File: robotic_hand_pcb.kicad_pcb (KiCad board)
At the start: 4 copper layers, 55 x 72.5 mm, 115 parts, among them J1 2171750001, J10 A6, J11 A7, J12 JST 1x5 Male, J13 JST 1x5 Male, J14 JST 1x5 Male, J15 JST 1x5 Male, J16 JST 1x5 Male, J2 TC2050-IDC, J4 UART, J5 A1, J6 A2, J7 A3, J8 A4, J9 A5, SW1 SPST, U1 LMR51430, U10 ACS712xLCTR-05B, U11 ACS712xLCTR-05B, U12 ACS712xLCTR-05B, U13 ACS712xLCTR-05B, U14 ULN2003ADR, U15 ULN2003ADR, U16 ULN2003ADR, U17 ULN2003ADR, U18 ULN2003ADR, U2 ld39150dt33-r, U3 TXB0104QPWRQ1, U4 STM32F446RET, U5 VL53L4CD, U7 BNO085, U8 ADS114S08, U9 ACS712xLCTR-05B, Y1 8M, Y2 32k768

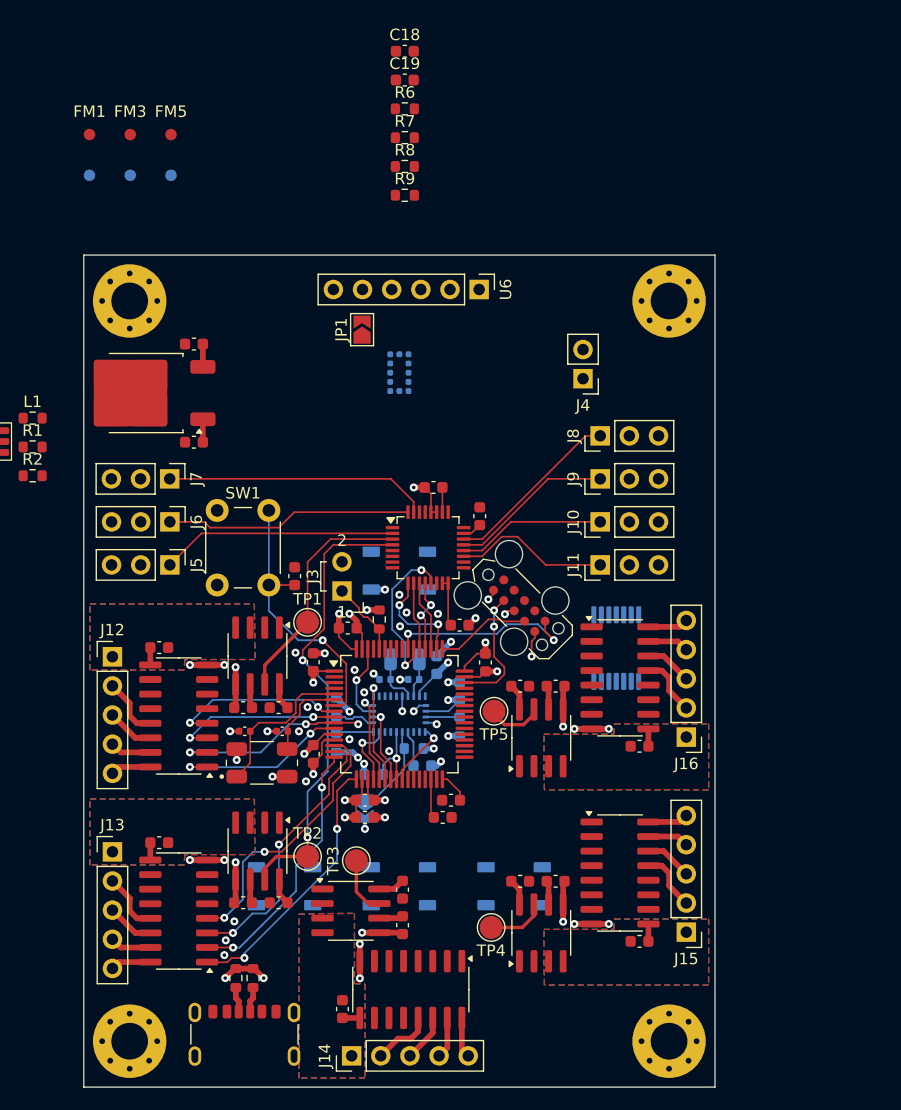
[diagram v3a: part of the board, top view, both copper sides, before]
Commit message: Update WIP, clean up stepper drivers
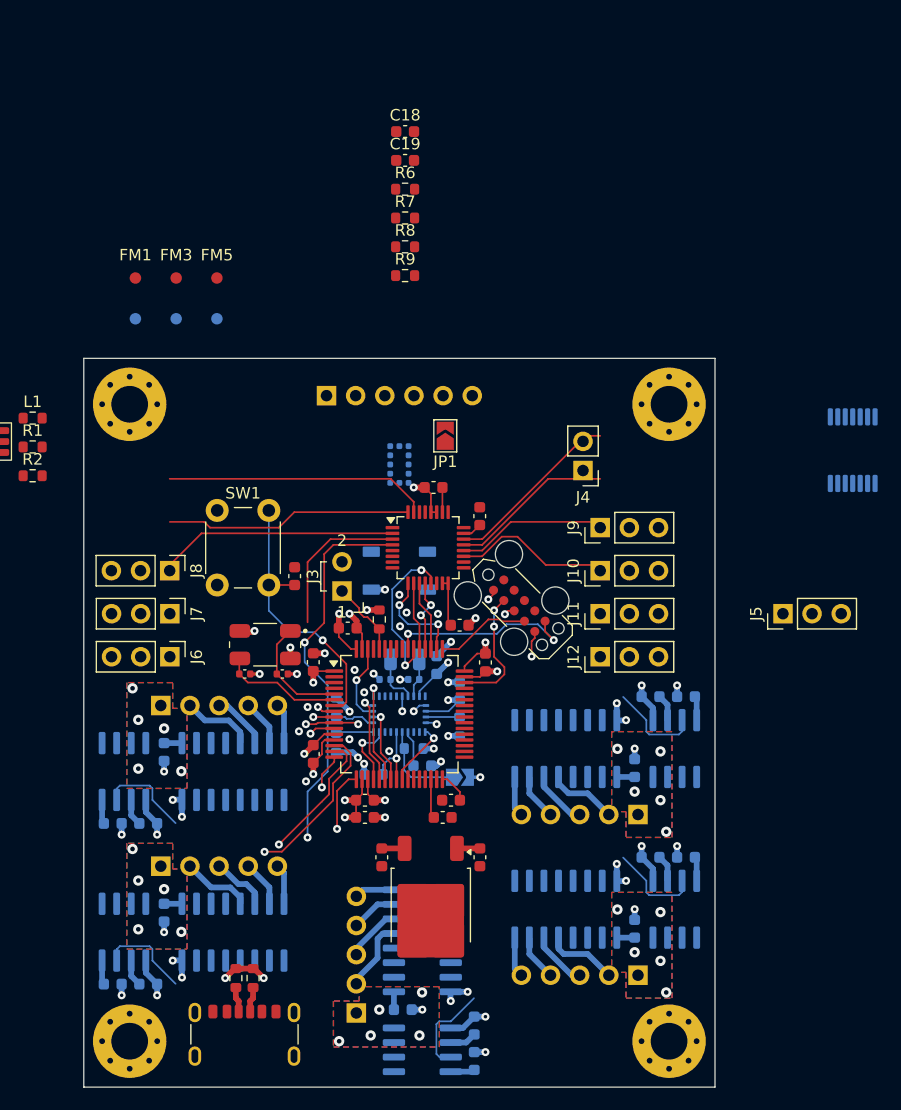
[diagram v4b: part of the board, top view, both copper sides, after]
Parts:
- removed D2, D3, D4: WS2812B, LED_SMD:LED_WS2812B_PLCC4_5.0x5.0mm_P3.2mm
- removed the J12 at (123.5, 100.0)
- removed the J16 at (173.5, 107.0)
- removed TP1, TP2, TP3, TP4, TP5: TestPoint, TestPoint:TestPoint_Pad_D2.0mm
- added J15: JST 1x5 Male, Connector_PinHeader_2.54mm:PinHeader_1x05_P2.54mm_Vertical, B.Cu at (144.8, 131.0)
- added J17: JST 1x5 Male, Connector_PinHeader_2.54mm:PinHeader_1x05_P2.54mm_Vertical, B.Cu at (169.3, 113.8)
- added J5: WS2812B, Connector_PinHeader_2.54mm:PinHeader_1x03_P2.54mm_Vertical, F.Cu at (181.9, 96.2)
- C28, C29, C30, C31, C32, C33, C34, C35, C36, C37, C38, C39, C40, C41, C42, J13, J14, U10, U11, U12, U13, U14, U15, U16, U17, U18, U6, U9: moved to B.Cu
- J16: renamed from J15; moved to B.Cu
- moved U2 51.2 mm to (151.2, 121.7), turned to -90 degrees
- moved C6 47.6 mm to (147.0, 117.5), turned to -90 degrees
- moved C5 43.9 mm to (155.5, 117.5), turned to -90 degrees
- moved U3 26.9 mm to (188.0, 82.0)
- moved J14 23.4 mm to (127.7, 118.2), turned to -90 degrees
- moved C28 17.6 mm to (123.5, 114.5), turned to 180 degrees
- moved U6 16.2 mm to (142.2, 77.2)
- moved C30 16.2 mm to (155.0, 135.2), turned to -90 degrees
- moved C29 16.1 mm to (123.5, 128.5), turned to 180 degrees
- moved U9 15.4 mm to (124.5, 110.0)
- moved C31 14.6 mm to (173.5, 117.5), turned to 0 degrees
- moved C32 14.5 mm to (173.5, 103.5), turned to 0 degrees
- moved U11 13.6 mm to (150.5, 134.2)
- moved U10 13.6 mm to (124.5, 124.0)
- moved J13 13.4 mm to (127.7, 104.2), turned to -90 degrees
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- renumbered J9 to J10, J10 to J11, J11 to J12, J5 to J6, J6 to J7, J7 to J8, J8 to J9
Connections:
- U14 pad 13: Net-(J12-Pin_2) -> Net-(J13-Pin_2)
- U14 pad 14: Net-(J12-Pin_3) -> Net-(J13-Pin_3)
- U14 pad 15: Net-(J12-Pin_4) -> Net-(J13-Pin_4)
- U14 pad 16: Net-(J12-Pin_5) -> Net-(J13-Pin_5)
- U15 pad 13: Net-(J13-Pin_2) -> Net-(J14-Pin_2)
- U15 pad 14: Net-(J13-Pin_3) -> Net-(J14-Pin_3)
- U15 pad 15: Net-(J13-Pin_4) -> Net-(J14-Pin_4)
- U15 pad 16: Net-(J13-Pin_5) -> Net-(J14-Pin_5)
- U16 pad 13: Net-(J14-Pin_2) -> Net-(J15-Pin_2)
- U16 pad 14: Net-(J14-Pin_3) -> Net-(J15-Pin_3)
- U16 pad 15: Net-(J14-Pin_4) -> Net-(J15-Pin_4)
- U16 pad 16: Net-(J14-Pin_5) -> Net-(J15-Pin_5)
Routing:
- net /M3_2: track 22.8 -> 3.09 mm, vias 2 -> 1
- net /M3_1: track 23.4 -> 5.42 mm, vias 2 -> 1
- net /M1_4: track 15.3 -> 1.58 mm, vias 2 -> 1
- net /M1_1: track 15.5 -> 2.26 mm, vias 2 -> 1
- net /M1_3: track 14.8 -> 1.82 mm, vias 2 -> 1
- net /M1_2: track 17.4 -> 4.83 mm, vias 3 -> 2
- net /M3_3: track 23.8 -> 11.5 mm, vias 2 -> 1
- net /M3_4: track 23.6 -> 14.3 mm, vias 2 -> 1
- net Net-(J15-Pin_2): track 0.00 -> 6.31 mm
- net GND: track 76.1 -> 81.4 mm, vias 55 -> 61
- net Net-(J12-Pin_2): track 5.30 -> 0.00 mm
- net Net-(J15-Pin_3): track 0.00 -> 4.88 mm
- net Net-(J12-Pin_3): track 4.12 -> 0.00 mm
- net Net-(J15-Pin_4): track 0.00 -> 4.04 mm
- net /HSE_IN: track 13.8 -> 9.98 mm
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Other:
- board size 55 x 72.5 mm -> 55 x 63.5 mm

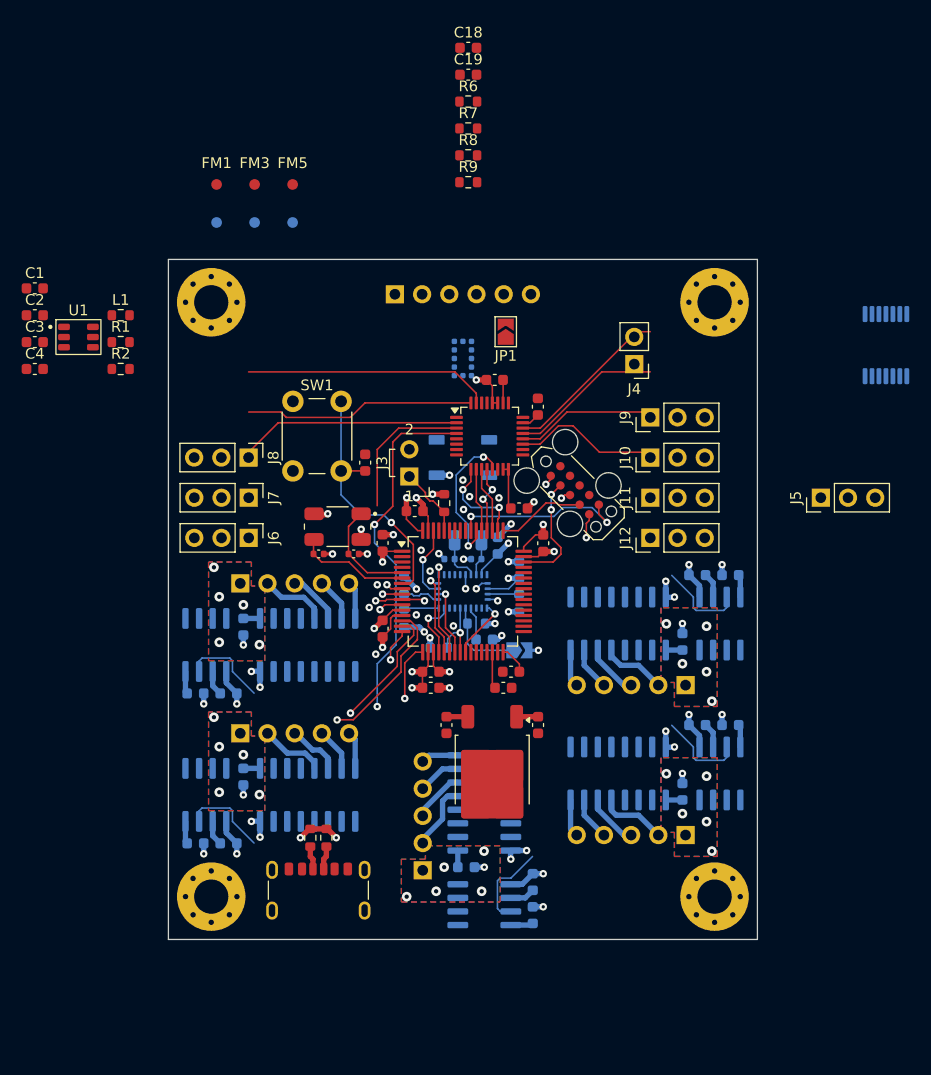
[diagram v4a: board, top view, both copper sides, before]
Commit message: Cleanup layout, add WIP routing
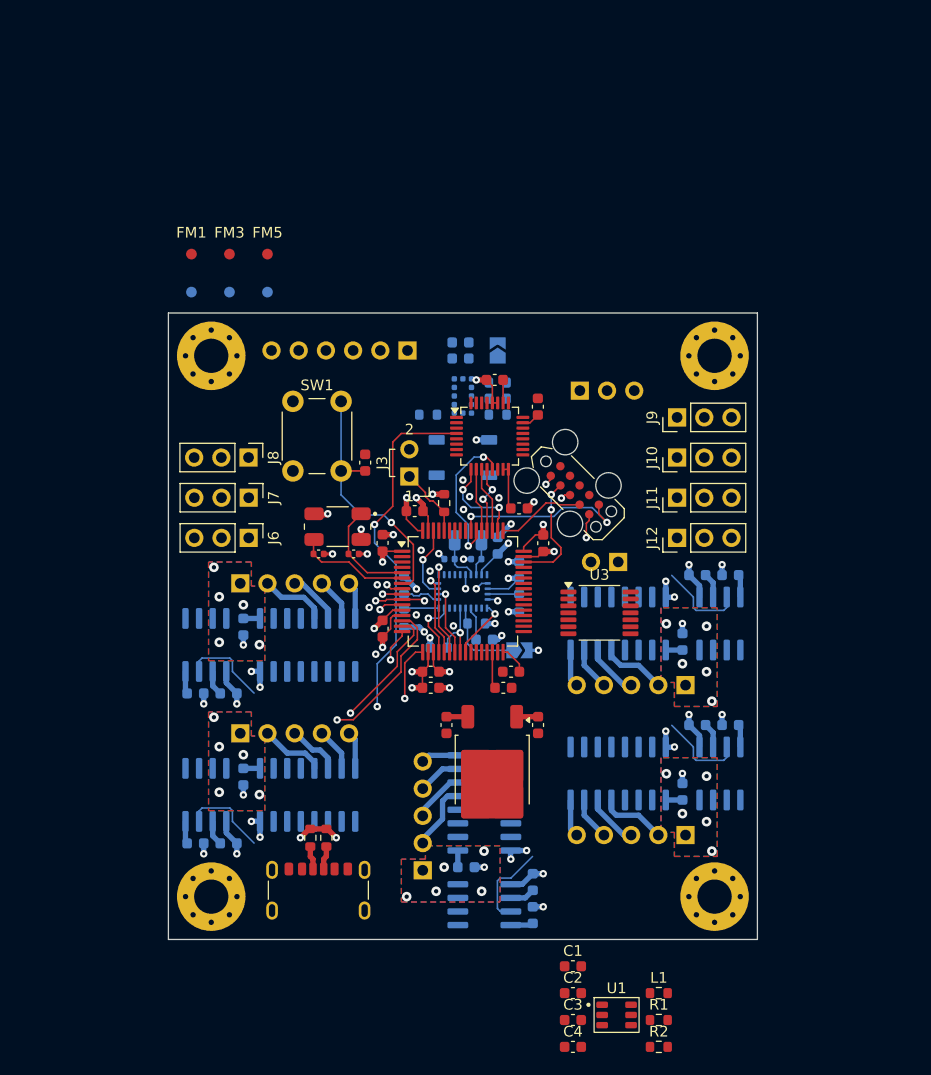
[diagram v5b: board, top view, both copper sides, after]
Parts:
- C18, C19, J4, J5, JP1, R6, R7, R8, R9: moved to B.Cu
- U3: moved to F.Cu
- moved C1 80.8 mm to (158.8, 140.0)
- moved C2 80.8 mm to (158.8, 142.5)
- moved C3 80.8 mm to (158.8, 145.0)
- moved C4 80.8 mm to (158.8, 147.5)
- moved R1 80.8 mm to (166.8, 145.0)
- moved U1 80.8 mm to (162.8, 144.6)
- moved L1 80.8 mm to (166.8, 142.5)
- moved R2 80.8 mm to (166.8, 147.5)
- moved U3 36.6 mm to (161.2, 107.0), turned to 0 degrees
- moved C18 29.0 mm to (148.3, 83.2)
- moved R6 27.9 mm to (151.8, 87.0), turned to 180 degrees
- moved C19 25.0 mm to (148.3, 81.8)
- moved J5 24.6 mm to (159.4, 86.2), turned to -90 degrees
- moved R8 24.5 mm to (145.2, 88.5)
- moved R7 23.9 mm to (151.8, 85.5)
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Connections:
- U3 pad 10: /TIM1_CH1_PWM_{5V} -> unconnected-(U3-B4-Pad10)
- U3 pad 13: unconnected-(U3-B1-Pad13) -> /TIM1_CH1_PWM_{5V}
- U3 pad 2: unconnected-(U3-A1-Pad2) -> /TIM1_CH1_PWM
- U3 pad 5: /TIM1_CH1_PWM -> unconnected-(U3-A4-Pad5)
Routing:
- net /robotic_hand_pcb_analog/ADC8: track 23.0 -> 0.00 mm
- net /robotic_hand_pcb_analog/ADC7: track 21.5 -> 0.00 mm
- net /robotic_hand_pcb_analog/ADC6: track 20.5 -> 0.00 mm
- net /robotic_hand_pcb_analog/ADC9: track 15.6 -> 0.00 mm
- net /robotic_hand_pcb_analog/ADC10: track 14.3 -> 0.00 mm
- net /robotic_hand_pcb_analog/ADC12: track 13.6 -> 0.00 mm
- net /robotic_hand_pcb_analog/ADC1: track 21.7 -> 8.17 mm
- net /robotic_hand_pcb_analog/ADC11: track 12.9 -> 0.00 mm
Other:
- board size 55 x 63.5 mm -> 55 x 58.5 mm

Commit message: Add minor layout improvements
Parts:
- J10, J11, J12, J6, J7, J8, J9: moved to B.Cu
- moved D1 18.9 mm to (164.5, 82.5)
- moved U3 17.6 mm to (163.5, 89.5), turned to 90 degrees
- moved C14 5.19 mm to (140.9, 88.0), turned to 90 degrees
- moved J5 4.81 mm to (159.0, 81.5), turned to 180 degrees
- moved J6 3.75 mm to (128.5, 96.2), turned to 90 degrees
- moved J7 3.75 mm to (128.5, 92.5), turned to 90 degrees
- moved J8 3.75 mm to (128.5, 88.8), turned to 90 degrees
- moved SW1 1.44 mm to (134.1, 93.8)
- turned J10 to -90 degrees
- turned J11 to -90 degrees
- turned J12 to -90 degrees
- turned J9 to -90 degrees
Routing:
- net /USART1_TX: track 0.00 -> 9.65 mm
- net /USART1_RX: track 0.00 -> 6.91 mm
- net /NRST: track 24.2 -> 22.5 mm

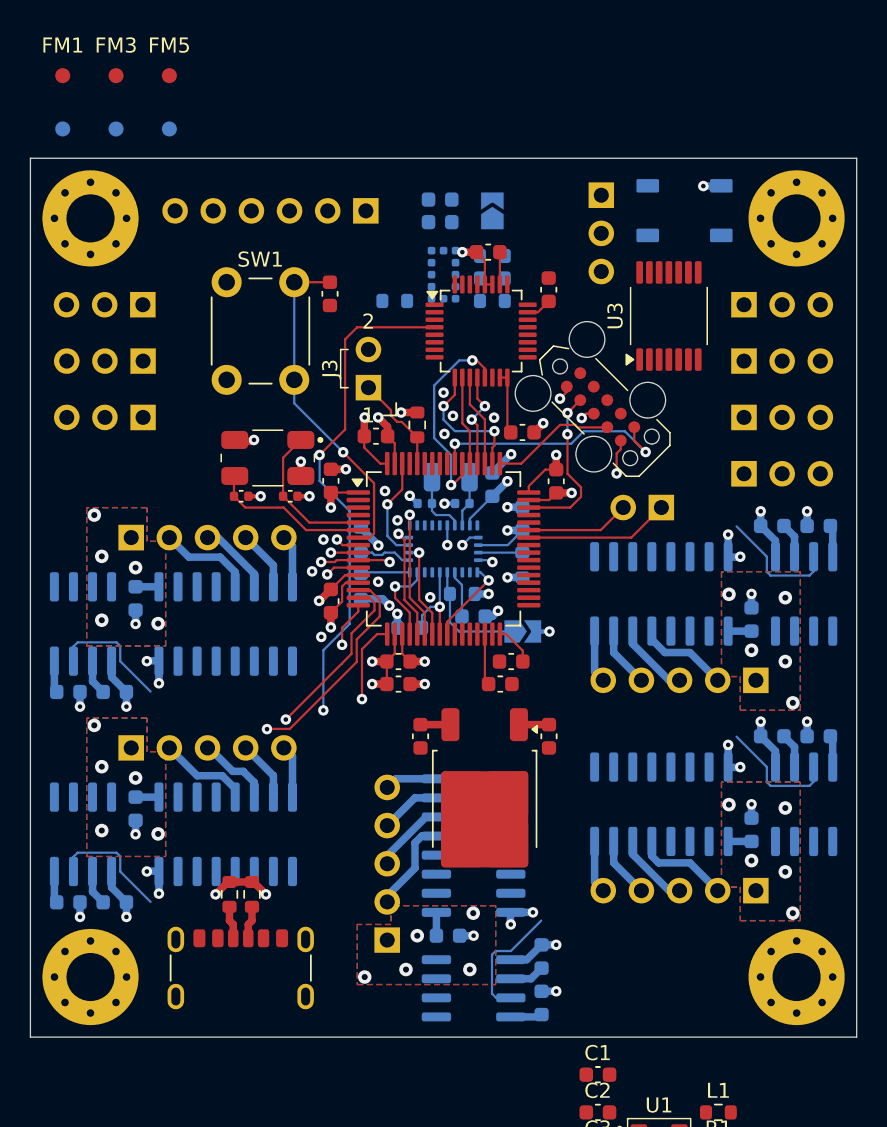
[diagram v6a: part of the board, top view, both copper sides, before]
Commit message: Route power, add major cleanup
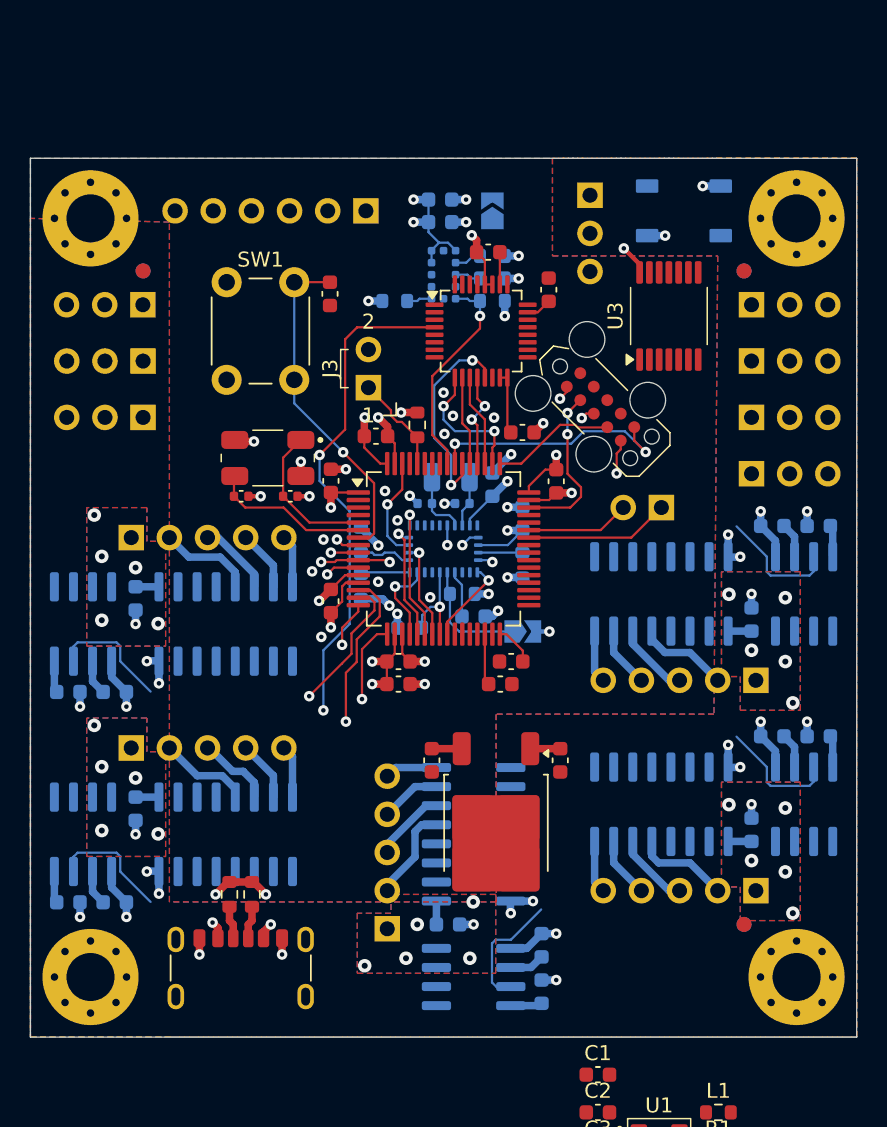
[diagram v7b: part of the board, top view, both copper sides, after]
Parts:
- FM2: moved to F.Cu
- FM5: moved to B.Cu
- moved FM3 70.3 mm to (168.5, 130.0)
- moved FM6 69.7 mm to (168.5, 130.0)
- moved FM4 42.9 mm to (168.5, 86.5)
- moved FM2 39.4 mm to (168.5, 86.5), turned to 0 degrees
- moved FM1 14.1 mm to (128.5, 86.5)
- moved FM5 13.1 mm to (128.5, 86.5), turned to 180 degrees
- moved C5 1.77 mm to (156.3, 119.1)
- moved C6 1.77 mm to (147.7, 119.1)
- moved U2 1.77 mm to (152.0, 123.3)
- moved C30 0.75 mm to (155.0, 134.5)
- moved C35 0.75 mm to (155.0, 131.4)
- moved C40 0.75 mm to (148.8, 130.0)
- moved J15 0.75 mm to (144.8, 130.3)
- moved J5 0.75 mm to (158.2, 81.5)
- moved U11 0.75 mm to (150.5, 133.5)
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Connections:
- C38 pad 1: +5V -> +5V_M1
- C39 pad 1: +5V -> +5V_M2
- C40 pad 1: +5V -> +5V_M3
- C41 pad 1: +5V -> +5V_M4
- C42 pad 1: +5V -> +5V_M5
- J13 pad 1: +5V -> +5V_M1
- J14 pad 1: +5V -> +5V_M2
- J15 pad 1: +5V -> +5V_M3
- J16 pad 1: +5V -> +5V_M4
- J17 pad 1: +5V -> +5V_M5
- U10 pad 3: +5V -> +5V_M2
- U10 pad 4: +5V -> +5V_M2
- U11 pad 3: +5V -> +5V_M3
- U11 pad 4: +5V -> +5V_M3
- U12 pad 3: +5V -> +5V_M4
- U12 pad 4: +5V -> +5V_M4
- U13 pad 3: +5V -> +5V_M5
- U13 pad 4: +5V -> +5V_M5
- U14 pad 9: +5V -> +5V_M1
- U15 pad 9: +5V -> +5V_M2
- U16 pad 9: +5V -> +5V_M3
- U17 pad 9: +5V -> +5V_M4
- U18 pad 9: +5V -> +5V_M5
- U9 pad 3: +5V -> +5V_M1
- U9 pad 4: +5V -> +5V_M1
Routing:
- net /EXTI4_TOF_INT: track 0.00 -> 14.2 mm, vias 0 -> 1
- net +3V3: track 44.6 -> 56.4 mm, vias 15 -> 21
- net GND: track 81.4 -> 85.8 mm, vias 61 -> 65
- net /M3_4: track 14.3 -> 10.7 mm
- net +5V: track 22.5 -> 20.3 mm, vias 25 -> 4
- net /M3_3: track 11.5 -> 9.25 mm
- net /I2C1_SCL: track 0.00 -> 1.81 mm
- net /I2C1_SDA: track 0.00 -> 1.73 mm
- net /GPIO_TOF_XSHUT: track 0.00 -> 1.69 mm
- net +5V_M5: track 0.00 -> 1.56 mm, vias 0 -> 5
- net +5V_M4: track 0.00 -> 1.56 mm, vias 0 -> 5
- net +5V_M3: track 0.00 -> 1.56 mm, vias 0 -> 5
- net +5V_M2: track 0.00 -> 1.56 mm, vias 0 -> 5
- net +5V_M1: track 0.00 -> 1.56 mm, vias 0 -> 5
- added copper zone on B.Cu, net +3V3
- added copper zone on F.Cu, net +3V3
- added copper zone on B.Cu, net +5V_M1
- added copper zone on F.Cu, net +5V_M1
- added copper zone on B.Cu, net +5V_M2
- added copper zone on F.Cu, net +5V_M2
- added copper zone on B.Cu, net +5V_M3
- added copper zone on F.Cu, net +5V_M3
- added copper zone on B.Cu, net +5V_M4
- added copper zone on F.Cu, net +5V_M4
- added copper zone on B.Cu, net +5V_M5
- added copper zone on F.Cu, net +5V_M5

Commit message: Near complete routing, cleanup
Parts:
- H1, H2, H3, H4: footprint MountingHole:MountingHole_3.2mm_M3_Pad_Via -> MountingHole:MountingHole_3.2mm_M3
- J1, R3, R4: moved to B.Cu
- J4: moved to F.Cu
- moved R4 33.7 mm to (167.8, 131.3)
- moved J1 26.5 mm to (161.5, 133.9), turned to 180 degrees
- moved C5 24.2 mm to (138.9, 136.0), turned to 180 degrees
- moved R3 20.8 mm to (156.5, 127.5)
- moved U2 19.3 mm to (134.7, 131.8), turned to 180 degrees
- moved C1 17.0 mm to (142.0, 142.5)
- moved C2 17.0 mm to (142.0, 145.0)
- moved C3 17.0 mm to (142.0, 147.5)
- moved C4 17.0 mm to (142.0, 150.0)
- moved U1 17.0 mm to (146.1, 147.1)
- moved L1 17.0 mm to (150.0, 145.0)
- moved R1 17.0 mm to (150.0, 147.5)
- moved R2 17.0 mm to (150.0, 150.0)
- moved FM2 13.3 mm to (180.8, 91.8)
- moved FM4 13.3 mm to (180.8, 91.8)
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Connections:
- U3 pad 10: unconnected-(U3-B4-Pad10) -> /TIM1_CH1_PWM_{5V}
- U3 pad 13: /TIM1_CH1_PWM_{5V} -> unconnected-(U3-B1-Pad13)
- U3 pad 2: /TIM1_CH1_PWM -> unconnected-(U3-A1-Pad2)
- U3 pad 5: unconnected-(U3-A4-Pad5) -> /TIM1_CH1_PWM
- U4 pad 33: /M5_4 -> /M5_1
- U4 pad 34: /M5_3 -> /M5_2
- U4 pad 35: /M5_2 -> /M5_3
- U4 pad 36: /M5_1 -> /M5_4
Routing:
- net /I2C1_SDA: track 1.73 -> 23.5 mm, vias 0 -> 1
- net /GPIO_TOF_XSHUT: track 1.69 -> 21.3 mm, vias 0 -> 1
- net /M3_2: track 3.09 -> 21.3 mm
- net /I2C1_SCL: track 1.81 -> 20.0 mm
- net /M5_4: track 0.00 -> 17.6 mm, vias 0 -> 1
- net /M5_3: track 0.00 -> 15.6 mm, vias 0 -> 1
- net /M4_4: track 0.00 -> 14.9 mm, vias 0 -> 1
- net /M3_3: track 9.25 -> 23.9 mm
- net /M3_4: track 10.7 -> 25.3 mm
- net /M5_2: track 0.00 -> 14.4 mm, vias 0 -> 1
- net /M3_1: track 5.42 -> 19.8 mm
- net /M4_3: track 0.00 -> 13.4 mm, vias 0 -> 1
- net /M5_1: track 0.00 -> 13.2 mm, vias 0 -> 1
- net Net-(JP1-B): track 0.00 -> 12.2 mm
- net /M4_2: track 0.00 -> 11.8 mm, vias 0 -> 1
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- added copper zone on B.Cu, net GND
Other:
- outline, holes or cut-outs redrawn
- board text added: "3V3"
- board text added: "GND"
- board text added: "INT"
- board text added: "SCL"
- board text added: "SDA"
- board text added: "XSHUT"
